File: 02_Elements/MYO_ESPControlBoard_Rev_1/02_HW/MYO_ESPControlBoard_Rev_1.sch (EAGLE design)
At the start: 48 parts, among them X2 332-06

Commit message: Updated Schematic and Board
Safe Bakcup
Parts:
- removed R_ESP3: 12KOhm, adafruit:R-US_M0805
- R_ESP0, R_ESP1: value 12KOhm -> 5KOhm
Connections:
- net BUZZER renamed GPIO26
- net MOT_SEN_1 renamed GPIO12
- removed net NRST: C_ESP_3.1, R_ESP3.1
- new net GPIO2: U_ESP.IO2
- net 3V3: no longer R_ESP3.2
- net EN: now also C_ESP_3.1
- net SWTAC_0: no longer U_ESP.IO2
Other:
- moved on the sheet: C_ESP_3

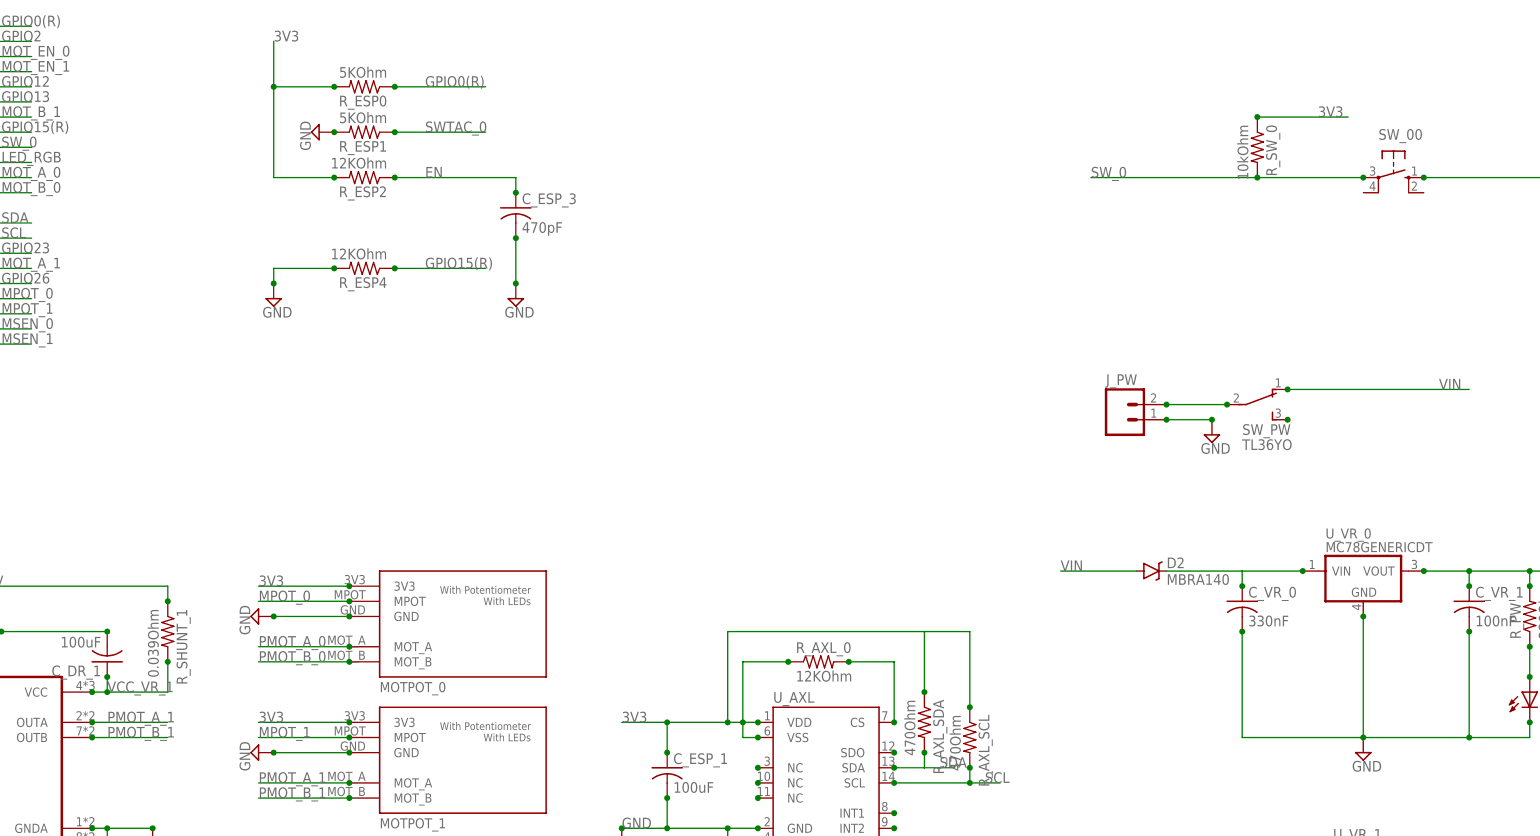
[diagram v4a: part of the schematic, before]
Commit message: Updated Dimension and Layout MYO_ESPControlBoard_Rev_1
Changes on MYO_ESPControlBoard_Rev_1:

- New Dimensions and Layout
- Changed Motor + Bracket Footprint
- Changed User Tactile Switch
- Added BOM in .txt format
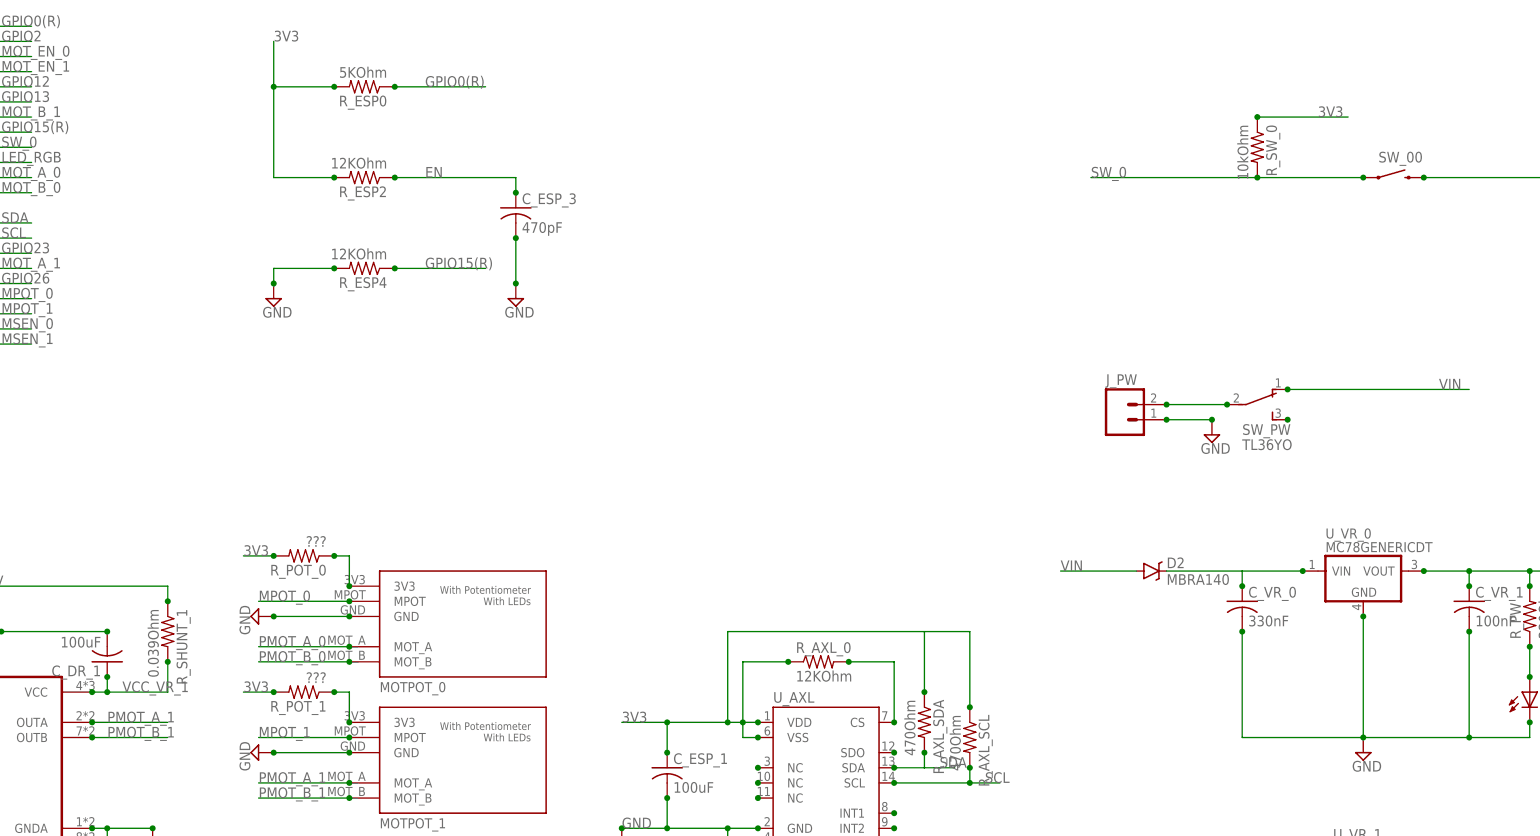
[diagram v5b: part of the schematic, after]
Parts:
- removed R_ESP1: 5KOhm, adafruit:R-US_M0805
- added R_POT_0, R_POT_1: ???, adafruit:R-US_M0805
- SW_00: value (none) -> SWITCH-MOMENTARY-2TACTILE-SWITCH-SMD-RIGHT-ANGLE; device switch-omron:10-XX -> SparkFun-Electromechanical:SWITCH-MOMENTARY-2TACTILE-SWITCH-SMD-RIGHT-ANGLE
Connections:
- removed net SWTAC_0: R_ESP1.1
- new net N$2: MOTPOT_0.3V3, R_POT_0.1
- new net N$3: MOTPOT_1.3V3, R_POT_1.1
- net 3V3: now also R_POT_0.2, R_POT_1.2; no longer MOTPOT_0.3V3, MOTPOT_1.3V3
- net GND: now also SW_00.2; no longer R_ESP1.2, SW_00.S
- net SW_0: now also SW_00.1; no longer SW_00.P
